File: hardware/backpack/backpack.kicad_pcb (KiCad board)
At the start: 2 copper layers, 31.7 x 110 mm, 89 parts, among them J1 Conn_01x14_Socket, J2 Conn_02x06_Top_Bottom, J3 Conn_02x06_Top_Bottom, J4 MIDI_TRS_A, J5 MIDI_TRS_A, J6 CONN 2x5 P=2.54mm, J7 USB_C, J8 MICROMOD-2222, J9 USB_C, Q2 2N7002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

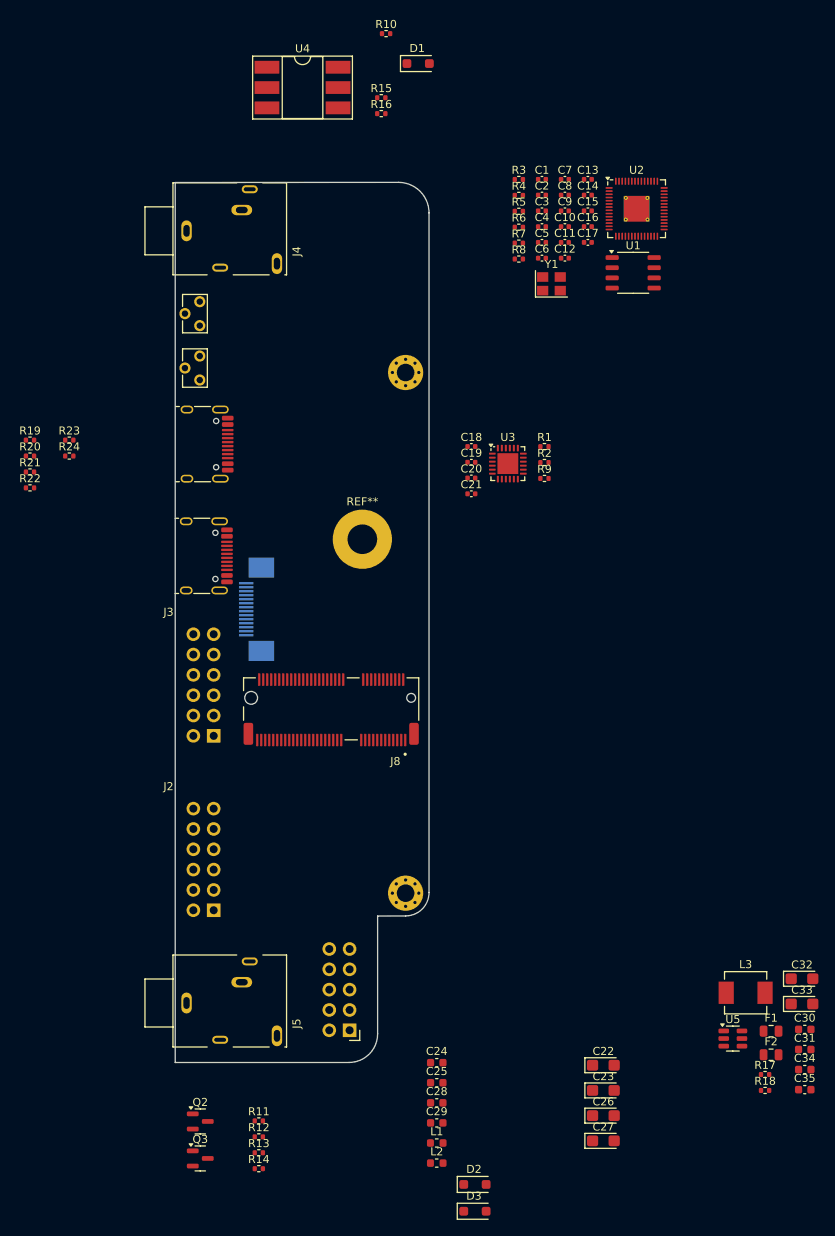
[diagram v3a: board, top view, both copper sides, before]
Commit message: connections + placement done
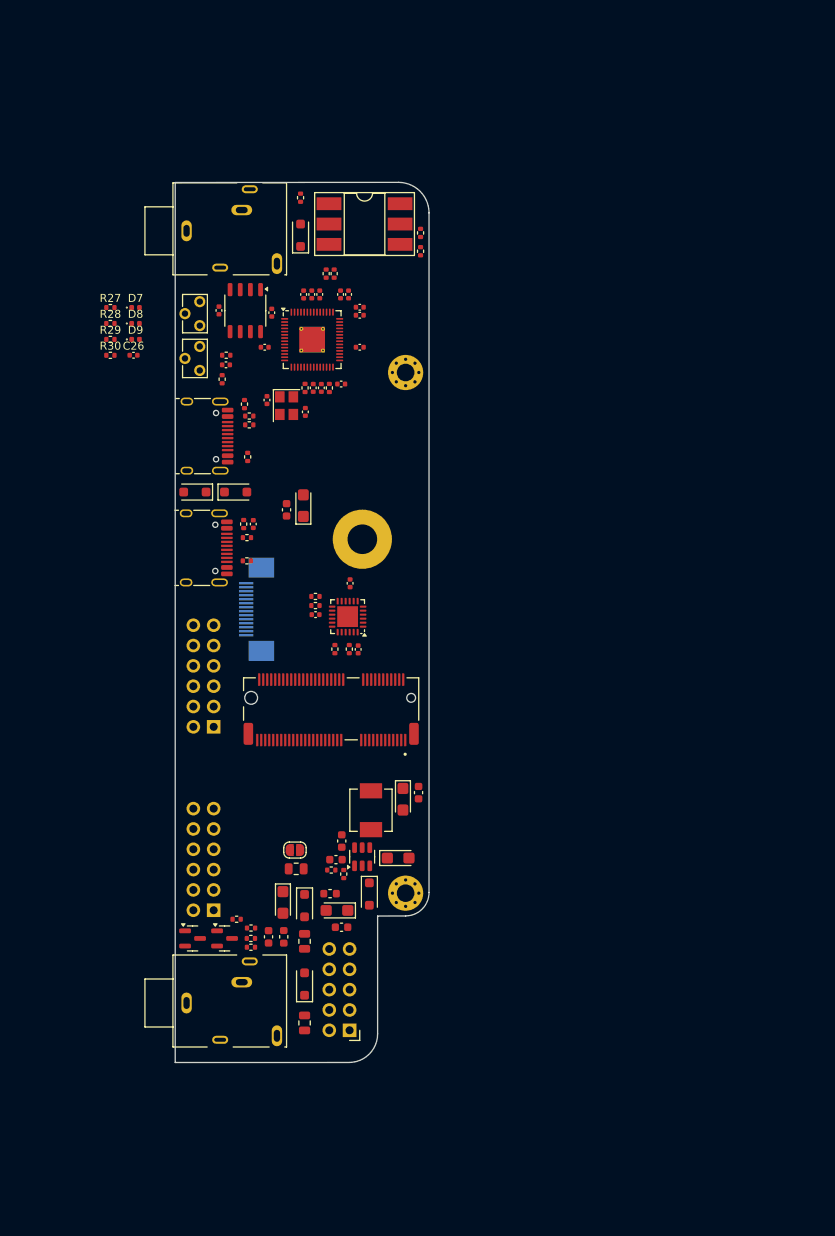
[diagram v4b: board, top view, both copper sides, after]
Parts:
- removed C27: 22.0uF, Capacitor_Tantalum_SMD:CP_EIA-3216-10_Kemet-I
- removed C28, C29: 100nF, Capacitor_SMD:C_0603_1608Metric
- added C36: 22.0uF, Capacitor_Tantalum_SMD:CP_EIA-3216-10_Kemet-I, F.Cu at (27.8, 84.5)
- added D4: 1N4007FL, Diode_SMD:D_SOD-123F, F.Cu at (2.39, 38.7)
- added D5: 1N4007FL, Diode_SMD:D_SOD-123F, F.Cu at (7.49, 38.7)
- added D6: 1N4007FL, Diode_SMD:D_SOD-123F, F.Cu at (24.2, 89.0)
- added D7: LED 0402 RED, LED_SMD:LED_0402_1005Metric, F.Cu at (-5.03, 15.6)
- added D8: LED 0402 RED, LED_SMD:LED_0402_1005Metric, F.Cu at (-5.03, 17.6)
- added D9: LED 0402 RED, LED_SMD:LED_0402_1005Metric, F.Cu at (-5.03, 19.6)
- added F3: 15V 200mA, Fuse:Fuse_0805_2012Metric, F.Cu at (15.1, 85.8)
- added JP1: ALLOW_USB_VIN, Jumper:SolderJumper-2_P1.3mm_Open_RoundedPad1.0x1.5mm, F.Cu at (14.9, 83.5)
- added R25: 27R/R0402, Resistor_SMD:R_0402_1005Metric, F.Cu at (17.5, 51.8)
- added R26: 27R/R0402, Resistor_SMD:R_0402_1005Metric, F.Cu at (17.5, 52.9)
- added R27: 10k, Resistor_SMD:R_0402_1005Metric, F.Cu at (-8.17, 15.6)
- added R28: 100R/R0402, Resistor_SMD:R_0402_1005Metric, F.Cu at (-8.17, 17.6)
- added R29: 100R/R0402, Resistor_SMD:R_0402_1005Metric, F.Cu at (-8.17, 19.6)
- added R30: 100R/R0402, Resistor_SMD:R_0402_1005Metric, F.Cu at (-8.17, 21.6)
- C26: value 22.0uF -> 0.1uF; footprint Capacitor_Tantalum_SMD:CP_EIA-3216-10_Kemet-I -> Capacitor_SMD:C_0402_1005Metric
- moved C26 111.7 mm to (-5.28, 21.6)
- moved C34 95.3 mm to (13.8, 40.9), turned to 90 degrees
- moved C33 88.1 mm to (15.9, 40.4), turned to 90 degrees
- moved C31 63.2 mm to (20.0, 84.7), turned to 180 degrees
- moved C30 62.5 mm to (20.8, 82.3), turned to 90 degrees
- moved C35 60.9 mm to (30.4, 76.3), turned to -90 degrees
- moved R17 59.9 mm to (19.4, 86.0), turned to 180 degrees
- moved F1 59.4 mm to (16.1, 94.9), turned to 90 degrees
- moved R18 59.2 mm to (21.0, 86.5), turned to 90 degrees
- moved F2 58.5 mm to (16.1, 105.1), turned to 90 degrees
- moved C32 54.7 mm to (28.4, 77.1), turned to -90 degrees
- moved L3 52.1 mm to (24.4, 78.5), turned to 90 degrees
- moved U5 51.6 mm to (23.3, 84.3), turned to 90 degrees
- moved U1 48.7 mm to (8.70, 16.0), turned to -90 degrees
- moved C17 47.8 mm to (6.28, 22.8), turned to 180 degrees
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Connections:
- C26 pad 1: GND -> ECP5_C4
- C26 pad 2: -12V -> GND
- J1 pad 1: /pmod_audio/SCL -> ECP5_C9
- J1 pad 2: /pmod_audio/SDA -> ECP5_D8
- J1 pad 3: /pmod_audio/PDN -> ECP5_C10
- J1 pad 4: /pmod_audio/MCLK -> ECP5_D9
- J1 pad 5: /pmod_audio/BICK -> ECP5_B11
- J1 pad 6: /pmod_audio/LRCK -> ECP5_C11
- J1 pad 7: /pmod_audio/SDOUT1 -> ECP5_D13
- J1 pad 8: /pmod_audio/SDIN1 -> ECP5_C13
- J2 pad 1: unconnected-(J2-Pin_1-Pad1) -> ECP5_A10
- J2 pad 10: unconnected-(J2-Pin_10-Pad10) -> ECP5_D16
- J2 pad 2: unconnected-(J2-Pin_2-Pad2) -> ECP5_B15
- J2 pad 3: unconnected-(J2-Pin_3-Pad3) -> ECP5_C15
- J2 pad 4: unconnected-(J2-Pin_4-Pad4) -> ECP5_C16
- J2 pad 7: unconnected-(J2-Pin_7-Pad7) -> ECP5_B10
- J2 pad 8: unconnected-(J2-Pin_8-Pad8) -> ECP5_A15
- J2 pad 9: unconnected-(J2-Pin_9-Pad9) -> ECP5_B16
- J3 pad 1: unconnected-(J3-Pin_1-Pad1) -> ECP5_A9
- J3 pad 10: unconnected-(J3-Pin_10-Pad10) -> ECP5_D14
- J3 pad 2: unconnected-(J3-Pin_2-Pad2) -> ECP5_A13
- J3 pad 3: unconnected-(J3-Pin_3-Pad3) -> ECP5_B14
- J3 pad 4: unconnected-(J3-Pin_4-Pad4) -> ECP5_C14
- J3 pad 7: unconnected-(J3-Pin_7-Pad7) -> ECP5_B9
- J3 pad 8: unconnected-(J3-Pin_8-Pad8) -> ECP5_B13
- J3 pad 9: unconnected-(J3-Pin_9-Pad9) -> ECP5_A14
- R1 pad 2: /usb/ULPI.~{RESET} -> ECP5_C7
- R11 pad 1: /midi/MIDI_TX -> ECP5_B8
- R16 pad 1: /midi/MIDI_RX -> ECP5_D5
- SW1 pad 1: unconnected-(SW1-Pad1) -> GND
- SW1 pad 2: unconnected-(SW1-Pad2) -> ECP5_C4
- U3 pad 1: /usb/ULPI.DIR -> ECP5_C6
- U3 pad 10: /usb/ULPI.DATA5 -> ECP5_A6
- U3 pad 11: /usb/ULPI.DATA6 -> ECP5_B6
- U3 pad 12: /usb/ULPI.DATA7 -> ECP5_B3
- U3 pad 13: /ULPI_USB_DP -> Net-(U3-DP)
- U3 pad 14: /ULPI_USB_DM -> Net-(U3-DM)
- U3 pad 21: /usb/ULPI.REFCLK -> ECP5_D7
- U3 pad 22: /usb/ULPI.~{RESET} -> ECP5_C7
- U3 pad 24: /usb/ULPI.STP -> ECP5_A2
- U3 pad 3: /usb/ULPI.NXT -> ECP5_C5
- U3 pad 4: /usb/ULPI.DATA0 -> ECP5_D6
- U3 pad 5: /usb/ULPI.DATA1 -> ECP5_D4
- U3 pad 6: /usb/ULPI.DATA2 -> ECP5_E4
- U3 pad 7: /usb/ULPI.DATA3 -> ECP5_A5
- U3 pad 8: /usb/ULPI.DATA4 -> ECP5_B5
- U5 pad 2: +12V -> /power/VAUX
- U5 pad 3: +12V -> /power/VAUX

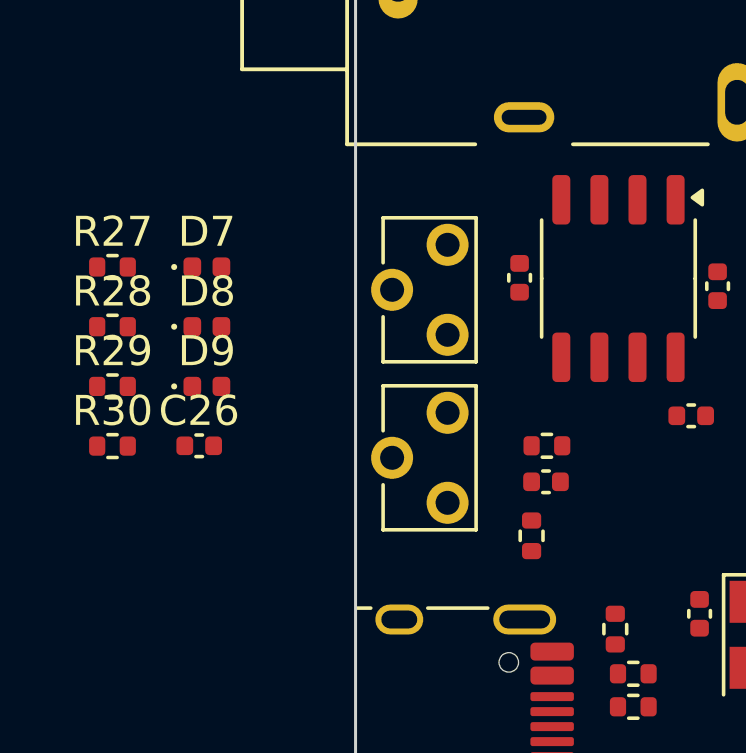
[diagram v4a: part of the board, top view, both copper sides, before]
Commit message: place 2 leds, route 2nd button to both FPGA and RP2040
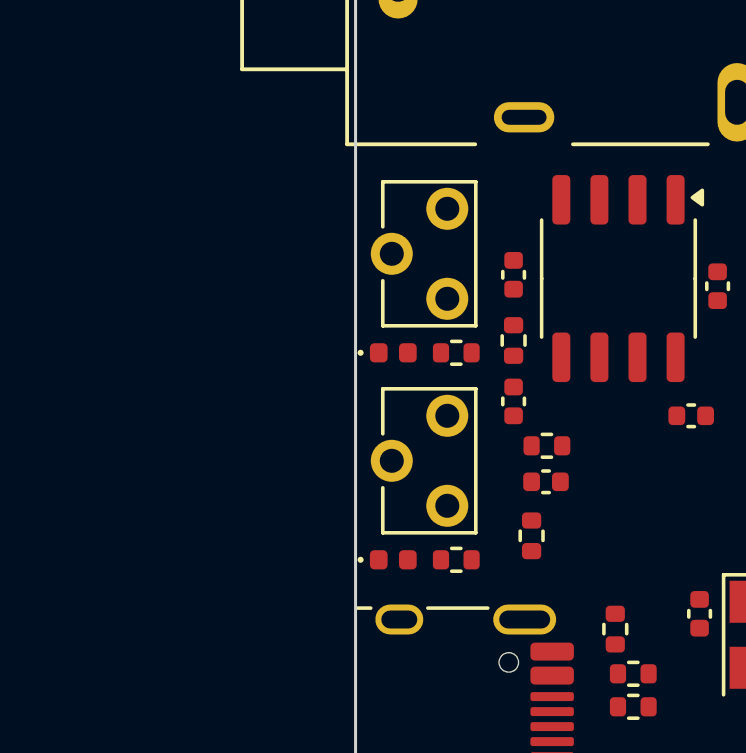
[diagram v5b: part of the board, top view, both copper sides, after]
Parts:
- removed D7: LED 0402 RED, LED_SMD:LED_0402_1005Metric
- removed R28: 100R/R0402, Resistor_SMD:R_0402_1005Metric
- moved R27 13.6 mm to (5.20, 18.1), turned to -90 degrees
- moved R30 12.1 mm to (3.29, 25.4)
- moved R29 11.5 mm to (3.29, 18.5)
- moved C26 10.6 mm to (5.20, 20.1), turned to -90 degrees
- moved D9 8.49 mm to (1.19, 25.4)
- moved D8 6.28 mm to (1.19, 18.5)
- moved SW1 1.20 mm to (2.99, 13.7)
- moved C1 0.22 mm to (5.20, 15.9)
- moved SW2 0.10 mm to (2.99, 20.6)
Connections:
- C17 pad 2: /rp2040_jtag/CSn -> ECP5_A7
- R3 pad 2: /rp2040_jtag/CSn -> ECP5_A7
- R8 pad 1: /rp2040_jtag/CSn -> ECP5_A7
- U1 pad 1: /rp2040_jtag/CSn -> ECP5_A7
- U2 pad 56: /rp2040_jtag/CSn -> ECP5_A7

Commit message: fix footprint errors and pin assignments on ffc
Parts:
- J1: value Conn_01x14_Socket -> Conn_01x15
- J4, J5: value MIDI_TRS_A -> AUDIO JACK PJ-324M0
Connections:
- J1 pad 1: ECP5_C9 -> -12V
- J1 pad 10: +3V3 -> ECP5_D9
- J1 pad 11: GND -> ECP5_B11
- J1 pad 12: +12V -> ECP5_C11
- J1 pad 13: unconnected-(J1-Pin_13-Pad13) -> ECP5_D13
- J1 pad 14: -12V -> ECP5_C13
- J1 pad 2: ECP5_D8 -> unconnected-(J1-Pin_2-Pad2)
- J1 pad 3: ECP5_C10 -> +12V
- J1 pad 4: ECP5_D9 -> GND
- J1 pad 5: ECP5_B11 -> +3V3
- J1 pad 6: ECP5_C11 -> GND
- J1 pad 7: ECP5_D13 -> ECP5_D8
- J1 pad 8: ECP5_C13 -> ECP5_C9
- J1 pad 9: GND -> ECP5_C10
- J4 pad SN: (no net) -> unconnected-(J4-PadSN)
- J5 pad SN: (no net) -> unconnected-(J5-PadSN)
- J8 pad S1: (no net) -> GND
- J8 pad S2: (no net) -> GND
- U3 pad 1: ECP5_C6 -> ECP5_A2
- U3 pad 24: ECP5_A2 -> ECP5_C6
